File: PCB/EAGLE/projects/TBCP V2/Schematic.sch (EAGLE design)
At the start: 110 parts, among them J1 FP Header, J2 12 Supply, J3 TB Header, Q1 DMP4025LK3Q-13, U1 ESP32-DEVKITC, U2 7805, U4 ADS1115, U5 TLE9201SG

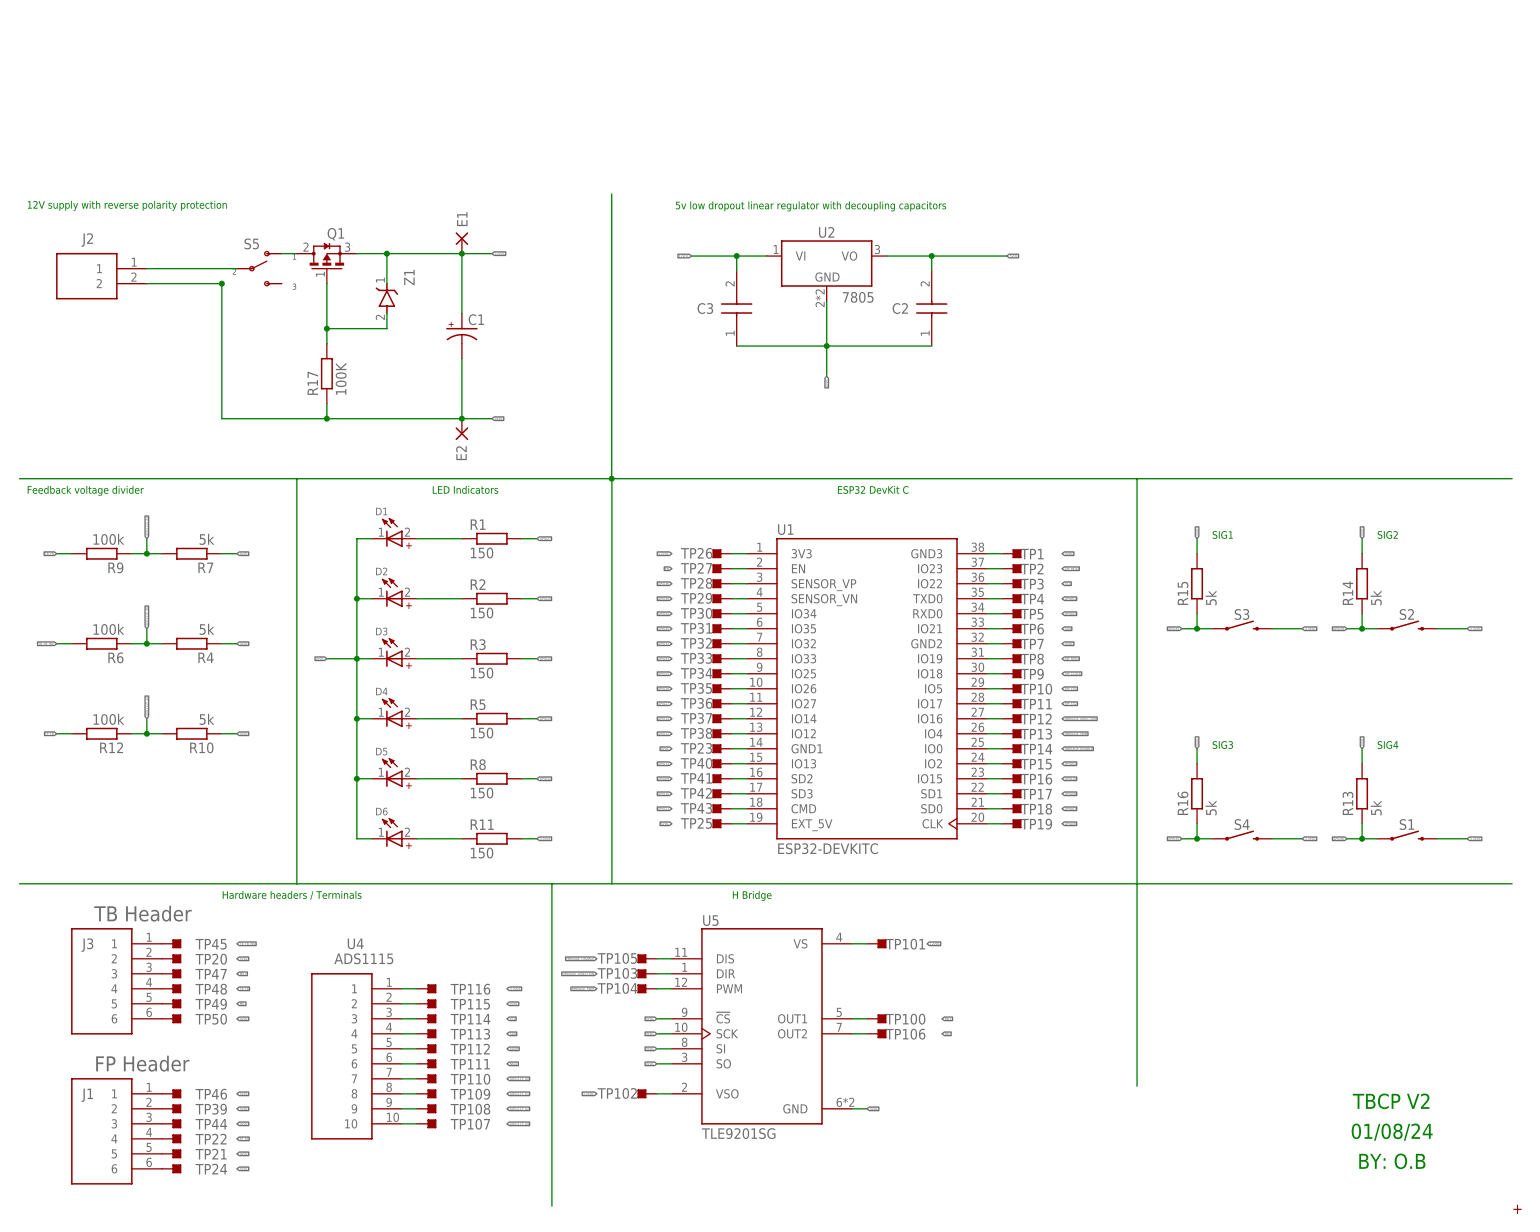
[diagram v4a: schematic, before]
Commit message: TBCP 2.0 sent to JLCPCB
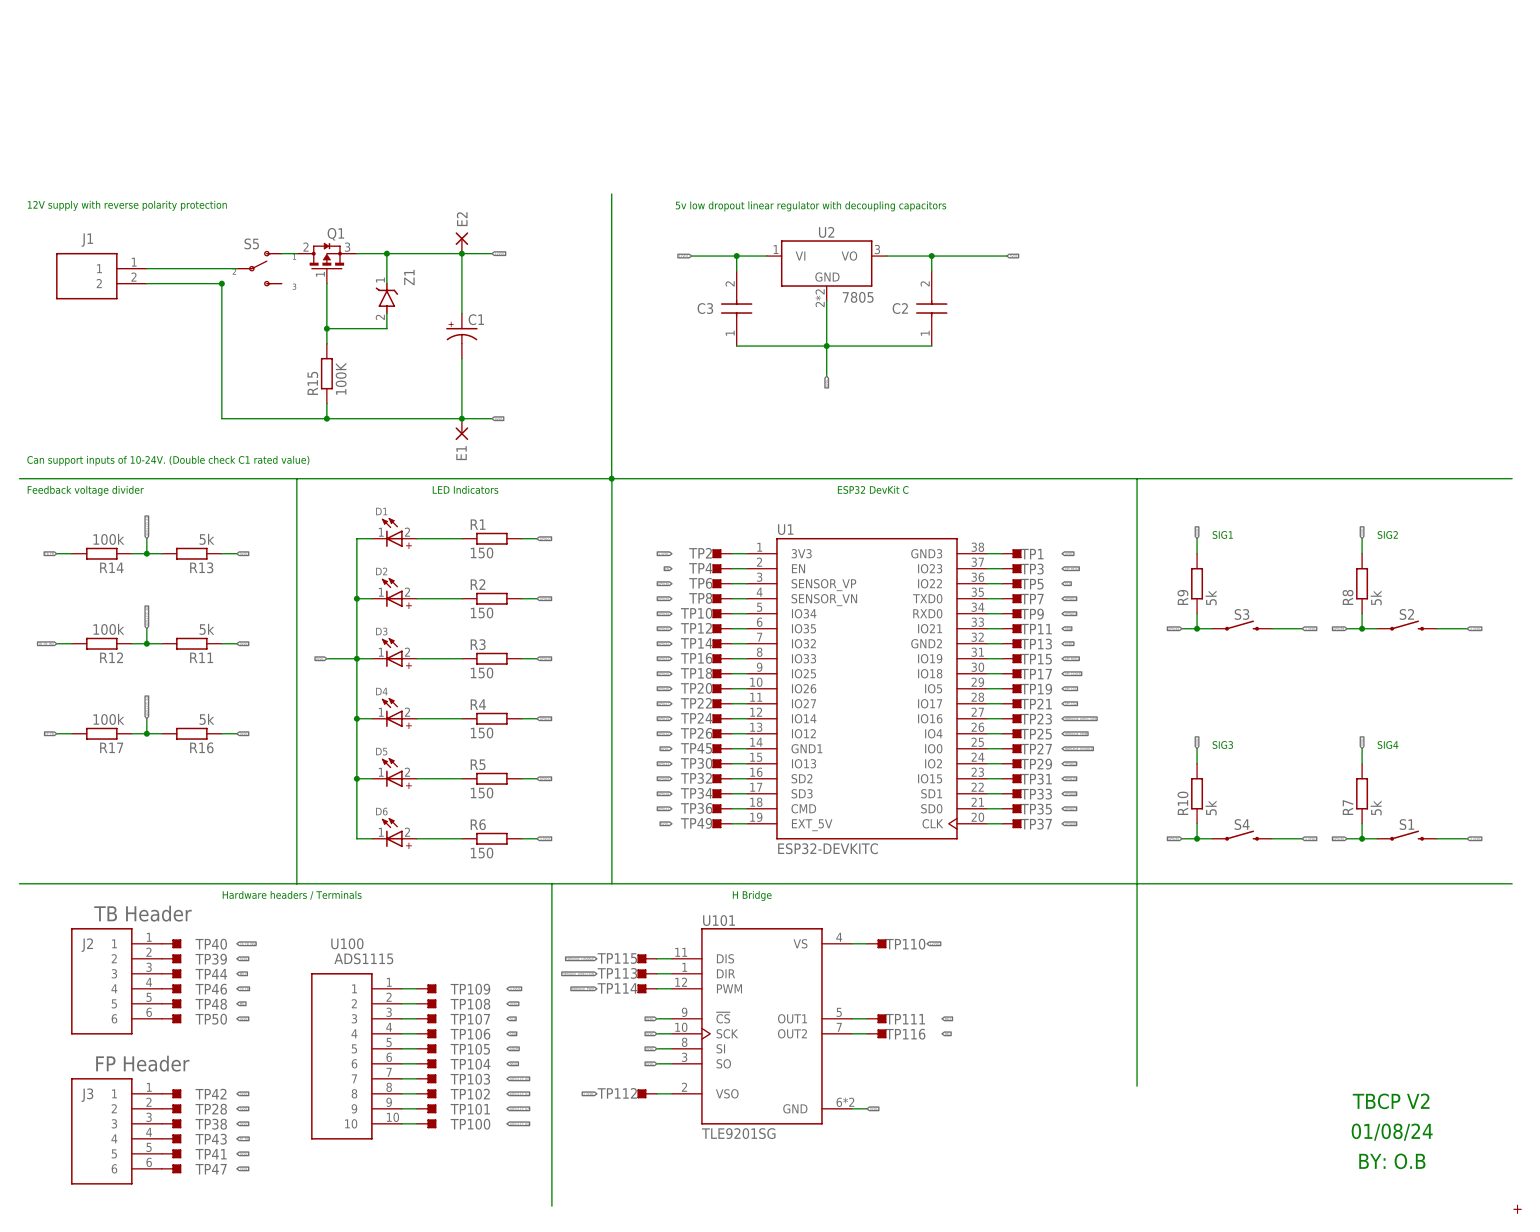
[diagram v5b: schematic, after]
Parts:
- C1: device BeagleBone_Blue_R3:CAPACITOR-PE3.5-8 -> BeagleBone_Blue_R3:CAPACITOR-PTAP5-80
- J1: value FP Header -> 12 Supply; device Terminal 5.08 Pitch 6S 1757284:1757284 -> Terminal 5.08 Pitch 2S :1757284
- J2: value 12 Supply -> TB Header; device Terminal 5.08 Pitch 2S :1757284 -> Terminal 5.08 Pitch 6S 1757284:1757284
- J3: value TB Header -> FP Header
- R11, R8: value 150 -> 5k
- R14: value 5k -> 100k
- R15: value 5k -> 100K
- R17: value 100K -> 100k
- R4: value 5k -> 150
- R6: value 100k -> 150
- R9: value 100k -> 5k
- TP10: value TESTPOINT_TPS-SMD-10SN -> GPIO34
- TP12: value TESTPOINT_TPS-SMD-10SN -> GPIO35
- TP14: value TESTPOINT_TPS-SMD-10SN -> GPIO32
- TP2: value TESTPOINT_TPS-SMD-10SN -> 3V3
- TP26: value 3V3 -> TESTPOINT_TPS-SMD-10SN
- TP27: value EN -> TESTPOINT_TPS-SMD-10SN
- TP28: value GPIO36 -> TESTPOINT_TPS-SMD-10SN
- TP29: value GPIO39 -> TESTPOINT_TPS-SMD-10SN
- TP30: value GPIO34 -> TESTPOINT_TPS-SMD-10SN
- TP31: value GPIO35 -> TESTPOINT_TPS-SMD-10SN
- TP32: value GPIO32 -> TESTPOINT_TPS-SMD-10SN
- TP4: value TESTPOINT_TPS-SMD-10SN -> EN
- TP6: value TESTPOINT_TPS-SMD-10SN -> GPIO36
- TP8: value TESTPOINT_TPS-SMD-10SN -> GPIO39
- renumbered U4 to U100, U5 to U101
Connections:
- net 0VDC: now also E1.P, J1.2, J2.6, J3.3, J3.5, R10.2, R11.1, R13.1, R15.1, R16.1, R7.2, R8.2, R9.2, TP108.TP, TP13.TP, TP28.TP, TP41.TP, TP45.TP; no longer E2.P, J1.3, J1.5, J2.2, J3.6, R10.1, R13.2, R14.2, R15.2, R16.2, R17.1, R4.1, R7.1, TP115.TP, TP21.TP, TP23.TP, TP39.TP, TP7.TP
- net 12VDC: now also E2.P, TP110.TP; no longer E1.P, TP101.TP
- net 3.3VDC: now also R6.2, TP109.TP, TP112.TP, TP2.TP; no longer R11.2, TP102.TP, TP116.TP, TP26.TP
- net 5VDC: now also J2.2, J3.1, J3.6, TP38.TP, TP39.TP, TP42.TP, TP47.TP, TP49.TP; no longer J1.1, J1.2, J1.6, TP20.TP, TP24.TP, TP25.TP, TP44.TP, TP46.TP
- net ADDR: now also TP105.TP; no longer TP112.TP
- net ADS1115_A0: now also R11.2, R12.1, TP103.TP; no longer R4.2, R6.1, TP110.TP
- net ADS1115_A1: now also R13.2, R14.1, TP102.TP; no longer R7.2, R9.1, TP109.TP
- net ADS1115_A2: now also R16.2, R17.1, TP101.TP; no longer R10.2, R12.1, TP108.TP
- net ADS1115_A4: now also TP100.TP; no longer TP107.TP
- net EN: now also TP4.TP; no longer TP27.TP
- net FP_FB: now also J3.4, R17.2, TP43.TP; no longer J1.4, R12.2, TP22.TP
- net GPIO01: now also TP7.TP; no longer TP4.TP
- net GPIO02: now also TP29.TP; no longer TP15.TP
- net GPIO03: now also TP9.TP; no longer TP5.TP
- net GPIO06: now also TP37.TP; no longer TP19.TP
- net GPIO07: now also TP35.TP; no longer TP18.TP
- net GPIO08: now also TP33.TP; no longer TP17.TP
- net GPIO09: now also TP32.TP; no longer TP41.TP
- net GPIO10: now also TP34.TP; no longer TP42.TP
- net GPIO11: now also TP36.TP; no longer TP43.TP
- net GPIO12: now also TP26.TP; no longer TP38.TP
- net GPIO13: now also TP30.TP; no longer TP40.TP
- net GPIO14: now also TP24.TP; no longer TP37.TP
- net GPIO15: now also TP31.TP; no longer TP16.TP
- net GPIO25: now also TP18.TP; no longer TP34.TP
- net GPIO26: now also TP20.TP; no longer TP35.TP
- net GPIO27: now also TP22.TP; no longer TP36.TP
- net GPIO32: now also R5.2, TP14.TP; no longer R8.2, TP32.TP
- net GPIO33: now also R4.2, TP16.TP; no longer R5.2, TP33.TP
- net GPIO34: now also R9.1, TP10.TP; no longer R15.1, TP30.TP
- net GPIO35: now also R10.1, TP12.TP; no longer R16.1, TP31.TP
- net GPIO36: now also R7.1, TP6.TP; no longer R13.1, TP28.TP
- net GPIO39: now also R8.1, TP8.TP; no longer R14.1, TP29.TP
- net HBRDIGE_DISABLE: now also TP115.TP, TP27.TP; no longer TP105.TP, TP14.TP
- net HBRIDGE_DIRECTION: now also TP113.TP, TP23.TP; no longer TP103.TP, TP12.TP
- net HBRIDGE_PWM: now also TP114.TP, TP25.TP; no longer TP104.TP, TP13.TP
- net M0+: now also J2.3, TP111.TP, TP44.TP; no longer J3.3, TP100.TP, TP47.TP
- net M0-: now also J2.5, TP116.TP, TP48.TP; no longer J3.5, TP106.TP, TP49.TP
- net N$1: now also J1.1; no longer J2.1
- net N$12: now also R4.1; no longer R5.1
- net N$13: now also R5.1; no longer R8.1
- net N$2: now also R6.1; no longer R11.1
- net N$41: now also TP104.TP; no longer TP111.TP
- net N$7: now also R15.2; no longer R17.2
- net SCL: now also TP107.TP, TP5.TP; no longer TP114.TP, TP3.TP
- net SDA: now also TP106.TP, TP11.TP; no longer TP113.TP, TP6.TP
- net SPI_CLOCK: now also TP17.TP; no longer TP9.TP
- net SPI_CS1: now also TP19.TP; no longer TP10.TP
- net SPI_CS2: now also TP21.TP; no longer TP11.TP
- net SPI_MISO: now also TP15.TP; no longer TP8.TP
- net SPI_MOSI: now also TP3.TP; no longer TP2.TP
- net TB_FB: now also J2.4, R14.2, TP46.TP; no longer J3.4, R9.2, TP48.TP
- net TB_FB_INV: now also J2.1, R12.2, TP40.TP; no longer J3.1, R6.2, TP45.TP
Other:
- note added: "Can support inputs of 10-24V. (Double check C1 rated value)"
- moved on the sheet: E1, E2, J3, R10, R11, R12, R13, R14, R15, R16, R17, R4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

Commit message: Added 3d Models to headers
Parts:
- S1, S2, S3, S4: value MOMENTARY-SWITCH-SPST-PTH-6.0MM-KIT -> MOMENTARY-SWITCH-SPST; device SparkFun-Switches:MOMENTARY-SWITCH-SPST-PTH-6.0MM-KIT -> 12mm TAC SWITCH:MOMENTARY-SWITCH-SPST
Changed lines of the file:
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@@
 <part name="C2" library="C0805C224J1RACTU" deviceset="C0805C224J1RACTU" device=""/>
 <part name="U$1" library="Wintec Logo" deviceset="WINTEC" device=""/>
-<part name="S5" library="500SSP1S1M6QEA" deviceset="500SSP1S1M6QEA" device=""/>
-<part name="S4" library="SparkFun-Switches" library_urn="urn:adsk.eagle:library:535" deviceset="MOMENTARY-SWITCH-SPST" device="-PTH-6.0MM-KIT" package3d_urn="urn:adsk.eagle:package:40170/2"/>
-<part name="S1" library="SparkFun-Switches" library_urn="urn:adsk.eagle:library:535" deviceset="MOMENTARY-SWITCH-SPST" device="-PTH-6.0MM-KIT" package3d_urn="urn:adsk.eagle:package:40170/2"/>
-<part name="S2" library="SparkFun-Switches" library_urn="urn:adsk.eagle:library:535" deviceset="MOMENTARY-SWITCH-SPST" device="-PTH-6.0MM-KIT" package3d_urn="urn:adsk.eagle:package:40170/2"/>
-<part name="S3" library="SparkFun-Switches" library_urn="urn:adsk.eagle:library:535" deviceset="MOMENTARY-SWITCH-SPST" device="-PTH-6.0MM-KIT" package3d_urn="urn:adsk.eagle:package:40170/2"/>
+<part name="S5" library="500SSP1S1M6QEA" deviceset="500SSP1S1M6QEA" device="" package3d_urn="urn:adsk.eagle:package:45039936/2"/>
+<part name="S4" library="12mm TAC SWITCH" deviceset="MOMENTARY-SWITCH-SPST" device="" package3d_urn="urn:adsk.eagle:package:45039953/2"/>
+<part name="S1" library="12mm TAC SWITCH" deviceset="MOMENTARY-SWITCH-SPST" device="" package3d_urn="urn:adsk.eagle:package:45039953/2"/>
+<part name="S2" library="12mm TAC SWITCH" deviceset="MOMENTARY-SWITCH-SPST" device="" package3d_urn="urn:adsk.eagle:package:45039953/2"/>
+<part name="S3" library="12mm TAC SWITCH" deviceset="MOMENTARY-SWITCH-SPST" device="" package3d_urn="urn:adsk.eagle:package:45039953/2"/>
 </parts>
 <sheets>
